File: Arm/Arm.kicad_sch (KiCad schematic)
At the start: 55 parts, among them J10 SparkMAX XT60 F, J11 CAN OUT, J12 SparkMAX XT60 F, J13 SparkMAX XT60 F, J14 Encoder 0, J2 Encoder Bundle, J3 CAN IN, J4 5V Swtich Power, J5 Power IN XT60 M, J6 SparkMAX XT60 F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

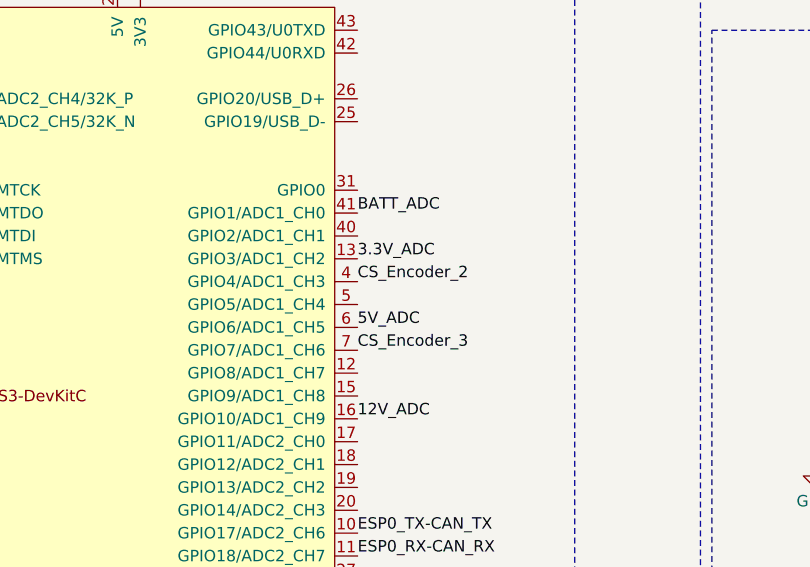
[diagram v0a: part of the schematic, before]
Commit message: Optimizations
Some Labesl

Mounting Holes

Changed some pins around for short traces
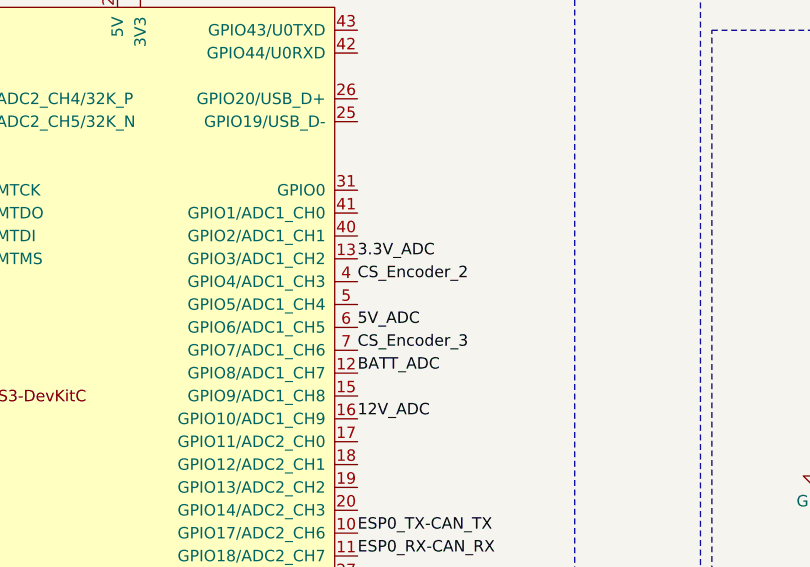
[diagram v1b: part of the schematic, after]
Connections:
- net BATT_ADC: now also U5.12 (GPIO8/ADC1_CH7); no longer U5.41 (GPIO1/ADC1_CH0)
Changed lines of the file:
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@@
+		)
+	)
+	(label "BATT_ADC"
+		(at 73.66 60.96 0)
+		(effects
+			(font
+				(size 1.27 1.27)
+			)
+			(justify left bottom)
 		)
 	)
@@
 		(effects
 			(font
-				(size 1.27 1.27)
-			)
-			(justify left bottom)
-		)
-	)
-	(label "BATT_ADC"
-		(at 73.66 43.18 0)
-		(effects
-			(font

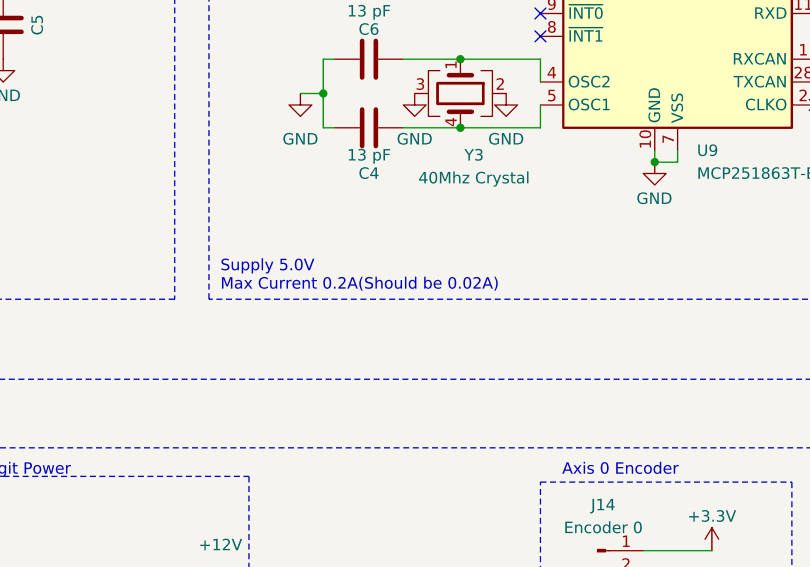
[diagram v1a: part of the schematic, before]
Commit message: Need to swtich to windows
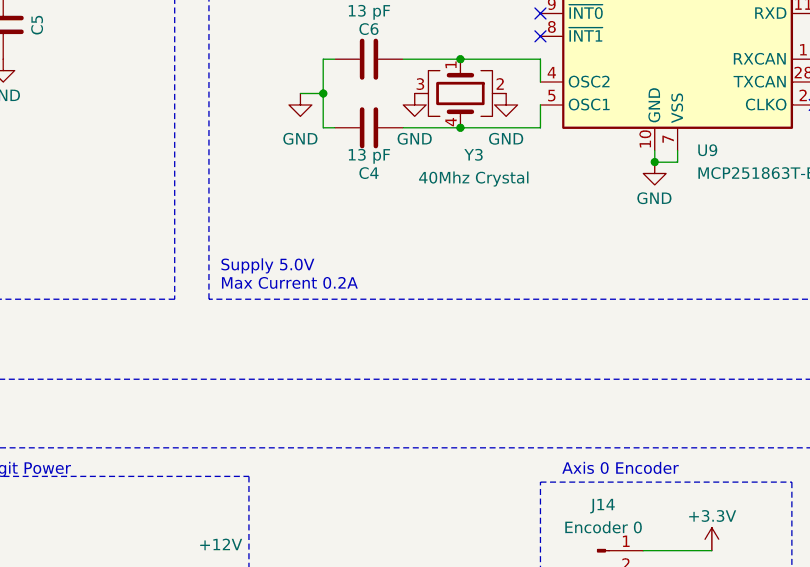
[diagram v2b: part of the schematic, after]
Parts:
- J10: footprint Connector_AMASS:AMASS_XT60-M_1x02_P7.20mm_Vertical -> Connector_AMASS:AMASS_XT60PW-F_1x02_P7.20mm_Horizontal
- J13: footprint Connector_AMASS:AMASS_XT60-F_1x02_P7.20mm_Vertical -> Connector_AMASS:AMASS_XT60PW-F_1x02_P7.20mm_Horizontal
- J5: footprint Connector_AMASS:AMASS_XT60PW-M_1x02_P7.20mm_Horizontal -> Connector_AMASS:AMASS_XT60-M_1x02_P7.20mm_Vertical
- J7: footprint Connector_AMASS:AMASS_XT60PW-F_1x02_P7.20mm_Horizontal -> Connector_AMASS:AMASS_XT60-F_1x02_P7.20mm_Vertical
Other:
- note added: "Supply 5.0V Max Current 0.2A"
- note removed: "Supply 5.0V Max Current 0.2A(Should be 0.02A)"

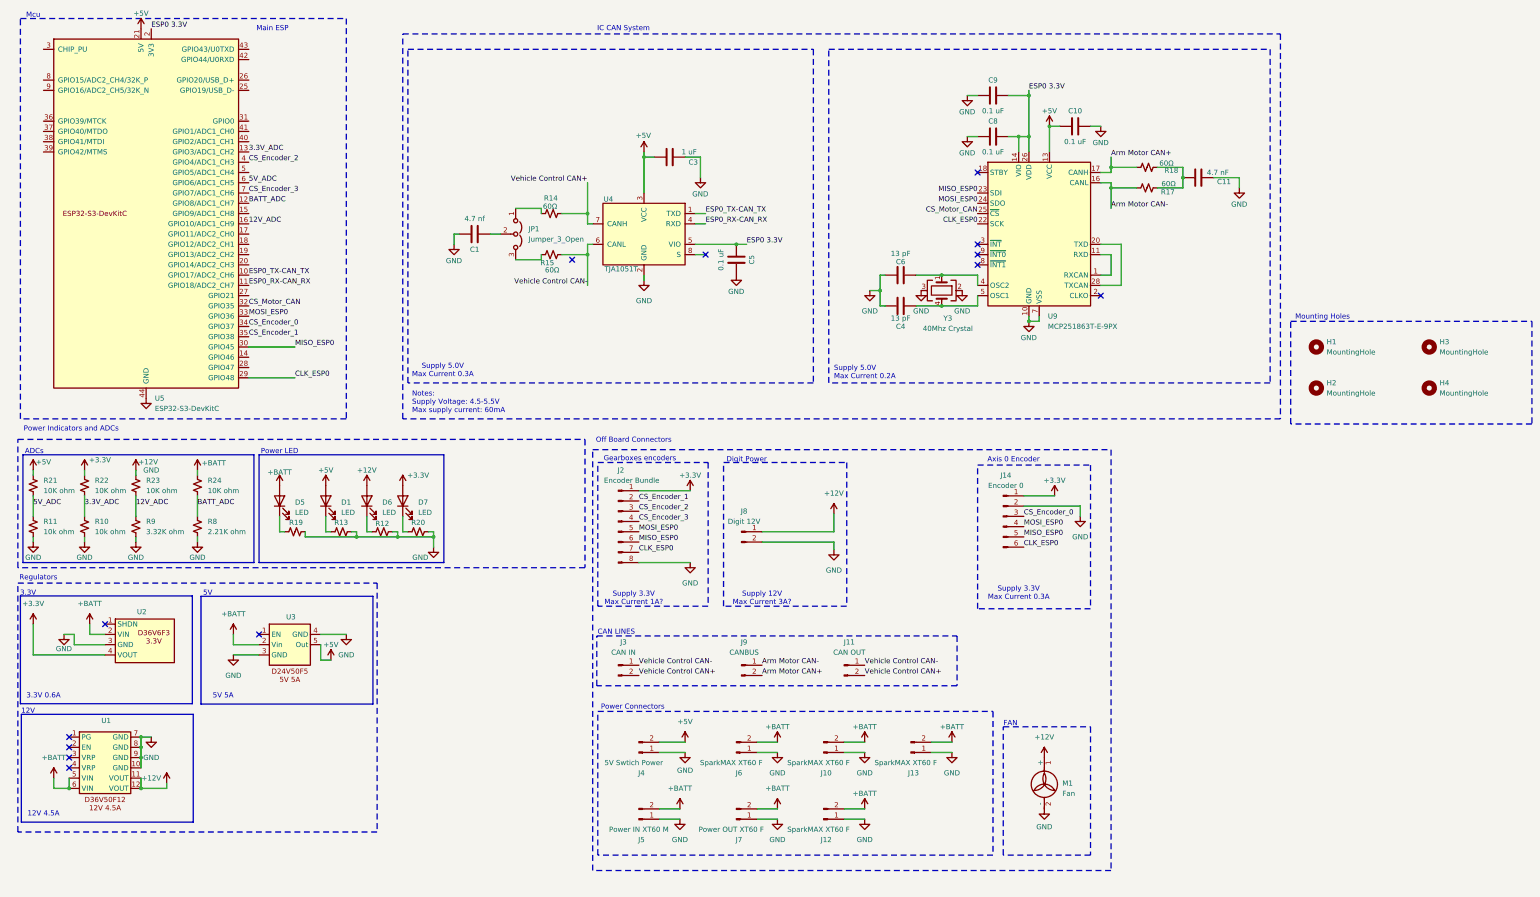
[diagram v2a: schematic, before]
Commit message: Moving Connectors and small layout changes
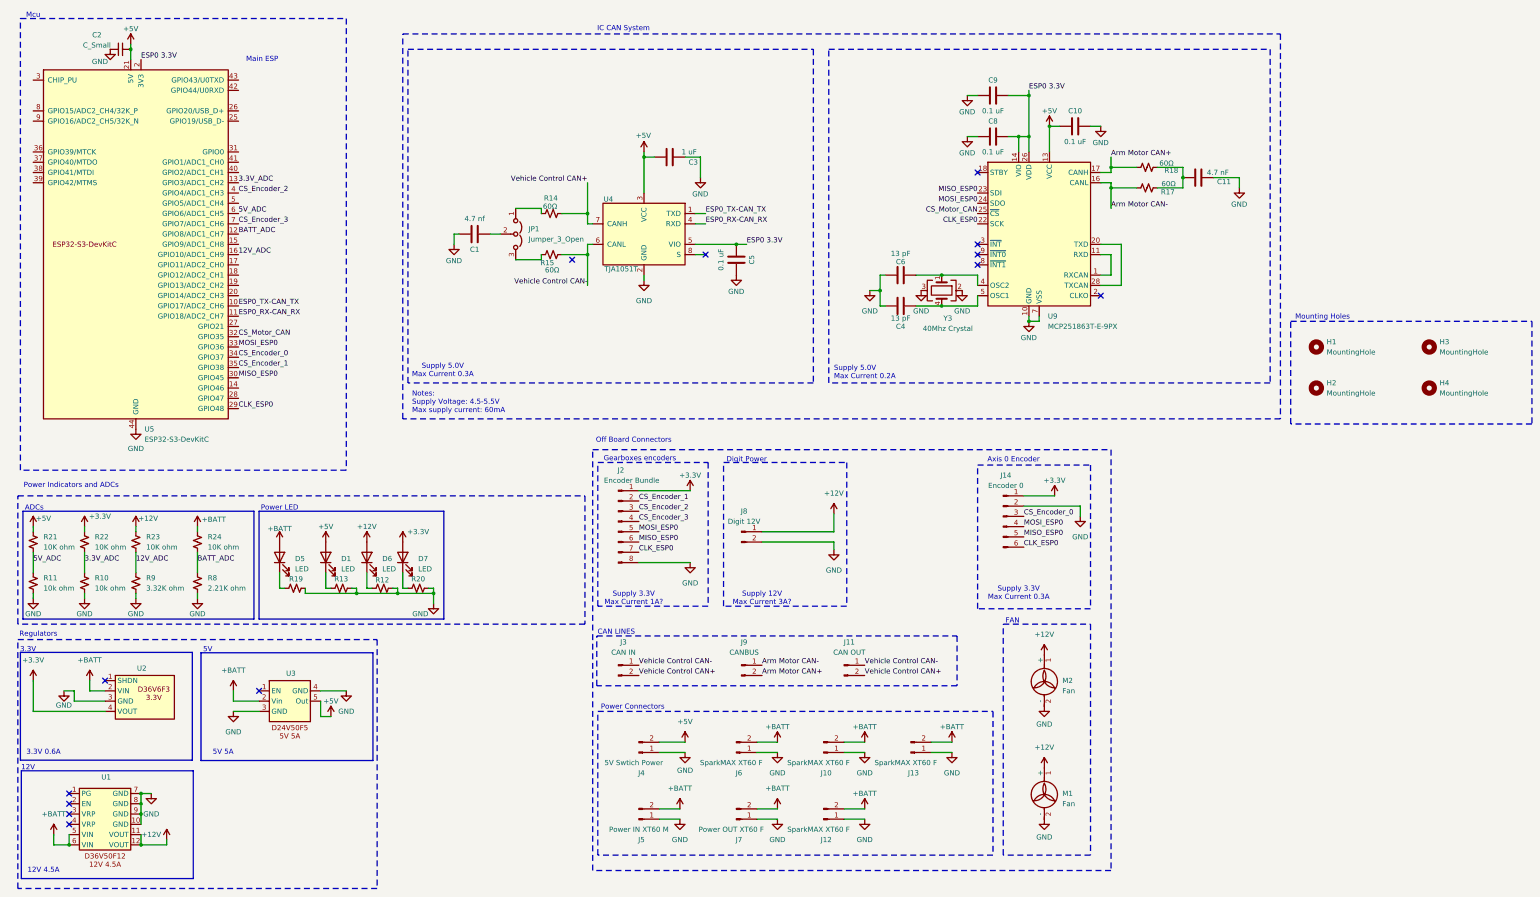
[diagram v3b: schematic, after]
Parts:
- added C2: C_Small, Capacitor_SMD:C_0603_1608Metric_Pad1.08x0.95mm_HandSolder, symbol Device:C_Small
- added M2: Fan, Connector_Molex:Molex_Mini-Fit_Jr_5566-02A_2x01_P4.20mm_Vertical, symbol Motor:Fan
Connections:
- net +12V: now also M2.1 (+)
- net +5V: now also C2.2
- net GND: now also C2.1, M2.2 (-)
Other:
- moved on the sheet: D1, D5, D6, D7, M1, R10, R11, R12, R13, R19, R20, R21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

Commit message: 1/3 Final Changes
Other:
- note added: "Bulk Caps"
- moved on the sheet: C10, C11, C4, C6, C8, C9, R17, R18, U9, Y3

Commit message: 2/3 Final Changes
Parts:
- added C12, C13, C14, C7: C_Small, Capacitor_SMD:C_Elec_4x5.8, symbol Device:C_Small
- J10, J13: footprint Connector_AMASS:AMASS_XT60PW-F_1x02_P7.20mm_Horizontal -> Connector_AMASS:AMASS_XT60-F_1x02_P7.20mm_Vertical
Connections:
- net +BATT: now also C12.1, C13.1, C14.1, C7.1
- net GND: now also C12.2, C13.2, C14.2, C7.2
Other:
- moved on the sheet: J14

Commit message: Final Part 3
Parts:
- removed C12, C13, C14, C7: C_Small, Capacitor_SMD:C_Elec_4x5.8, symbol Device:C_Small
- added C12, C13, C14, C7: 63uF, Capacitor_SMD:CP_Elec_6.3x7.7, symbol Device:C_Polarized_Small
- J12, J6: footprint Connector_AMASS:AMASS_XT60PW-F_1x02_P7.20mm_Horizontal -> Connector_AMASS:AMASS_XT60-F_1x02_P7.20mm_Vertical
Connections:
- net +BATT: now also C12.1, C13.1, C14.1, C7.1
- net GND: now also C12.2, C13.2, C14.2, C7.2

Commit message: Review Changes
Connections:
- net CLK_ESP0: no longer U5.29 (GPIO48)
- net MISO_ESP0: no longer U5.30 (GPIO45)
- net MOSI_ESP0: no longer U5.33 (GPIO36), U9.24 (SDO)
- new net SPI_CLK: U5.29 (GPIO48)
- new net SPI_MISO: U5.30 (GPIO45)
- new net SPI_MOSI: U5.33 (GPIO36)
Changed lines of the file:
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@@
 			"AAAAAAAAAAAAAAAAAAAAAAAAAAAAAAAAAAAAAAAAAAAAAAAAAAAAAAAAAAAAAAAAAAAAAAAAAAAA"
 			"AAAAAAAAAAAAAAAAAAAAAAAAAAAAAAAAAAAAAAAAAAAAAAAAAAAAAAAAAAAAAAAAAAAAAAAAAAAA"
+			"AAAAAAAAAAAAAAAAAAAAAAAAAAAAAAAAAAAAAAAAAAAAAAAAAAAAAAAAAAAAAAAAAAAAAAAAAAAA"
+			"AAAAAAAAAAAAAAAAAAAAAAAAAAAAAAAAAAAAAAAAAAAAAAAAAAAAAAAAAAAAAAAAAAAAAAAAAAAA"
+			"AAAAAAAAAAAAAAAAAAAAAAAAAAAAAAAAAAAAAAAAAAAAAAAAAAAAAAAAAAAAAAAAAAAAAAAAAAAA"
+			"AAAAAAAAAAAAAAAAAAAAAAAAAAAAAAAAAAAAAAAAAAAAAAAAAAAAAAAAAAAAAAAAAAAAAAAAAAAA"
+			"AAAAAAAAAAAAAAAAAAAAAAAAAAAAAAAAAAAAAAAAAAAAAAAAAAAAAAAAAAAAAAAAAAAAAAAAAAAA"
+			"AAAAAAAAAAAAAAAAAAAAAAAAAAAAAAAAAAAAAAAAAAAAAAAAAAAAAAAAAAAAAAAAAAAAAAAAAAAA"
+			"AAAAAAAAAAAAAAAAAAAAAAAAAAAAAAAAAAAAAAAAAAAAAAAAAAAAAAAAAAAAAAAAAAAAAAAAAAAA"
+			"AAAAAAAAAAAAAAAAAAAAAAAAAAAAAAAAAAAAAAAAAAAAAAAAAAAAAAAAAAAAAAAAAAAAAAAAAAAA"
+			"AAAAAAAAAAAAAAAAAAAAAAAAAAAAAAAAAAAAAAAAAAAAAAAAAAAAAAAAAAAAAAAAAAAAAAAAAAAA"
+			"AAAAAAAAAAAAAAAAAAAAAAAAAAAAAAAAAAAAAAAAAAAAAAAAAAAAAAAAAAAAAAAAAAAAAAAAAAAA"
+			"AAAAAAAAAAAAAAAAAAAAAAAAAAAAAAAAAAAAAAAAAAAAAAAAAAAAAAAAAAAAAAAAAAAAAAAAAAAA"
+			"AAAAAAAAAAAAAAAAAAAAAAAAAAAAAAAAAAAAAAAAAAAAAAAAAAAAAAAAAAAAAAAAAAAAAAAAAAAA"
+			"AAAAAAAAAAAAAAAAAAAAAAAAAAAAAAAAAAAAAAAAAAAAAAAAAAAAAAAAAAAAAAAAAAAAAAAAAAAA"
+			"AAAAAAAAAAAAAAAAAAAAAAAAAAAAAAAAAAAAAAAAAAAAAAAAAAAAAAAAAAAAAAAAAAAAAAAAAAAA"
+			"AAAAAAAAAAAAAAAAAAAAAAAAAAAAAAAAAAAAAAAAAAAAAAAAAAAAAAAAAAAAAAAAAAAAAAAAAAAA"
+			"AAAAAAAAAAAAAAAAAAAAAAAAAAAAAAAAAAAAAAAAAAAAAAAAAAAAAAAAAAAAAAAAAAAAAAAAAAAA"
+			"AAAAAAAAAAAAAAAAAAAAAAAAAAAAAAAAAAAAAAAAAAAAAAAAAAAAAAAAAAAAAAAAAAAAAAAAAAAA"
+			"AAAAAAAAAAAAAAAAAAAAAAAAAAAAAAAAAAAAAAAAAAAAAAAAAAAAAAAAAAAAAAAAAAAAAAAAAAAA"
 			"AAAAAAAAAAAAAAAAAAAAAAAAAAAAAAAAAAAAAAAAAAAAAAAAAAAAAAAAAA=="
 		)
@@
 			"AAAAZAAAAGUAAABOAAAAdAAAAFMAAAA4AAAAYgAAAGEAAAAxAAAANAAAADQAAABzAAAAZAAAAEkA"
 			"AABuAAAAbQAAADAAAABJAAAAKwAAAEgAAAA5AAAAWgAAADAAAABrAAAAWAAAAHkAAAA3AAAAZgAA"
-			"AEsAAAArAAAAMwAAAFMAAAB3AAAAbwAAAFUAAABoAAAANQAAAE8AAABkAAAAegAAAA=="
+			"AEsAAAArAAAAMwAAAFMAAAB3AAAAbwAAAFUAAABoAAAANQAAAE8AAABkAAAAegAAAFoAAABHAAAA"
+			"TwAAAE0AAABjAAAAOQAAAGEAAAArAAAARgAAAGYAAABGAAAAUAAAAGgAAABYAAAAeAAAAEQAAAA0"
+			"AAAASQAAADEAAAArAAAAOAAAADgAAABLAAAAKwAAAEsAAAA3AAAARwAAAFQAAABUAAAAZAAAAFcA"
+			"AAAwAAAAOQAAAHgAAABIAAAAYwAAADIAAABzAAAAMgAAAE4AAAA4AAAAVAAAAEYAAABRAAAAdwAA"
+			"AEIAAAAyAAAAawAAAGoAAAA3AAAAcAAAAEIAAAA2AAAAMQAAAEcAAABFAAAANAAAAFMAAAA0AAAA"
+			"ZgAAAHgAAABPAAAAWQAAADQAAAByAAAATAAAADUAAABVAAAAYQAAAGIAAABVAAAAVgAAAEYAAABw"
+			"AAAAUgAAAHUAAABwAAAASwAAAC8AAABOAAAAegAAAFgAAAA5AAAANQAAAHUAAAA2AAAAYQAAAFgA"
+			"AABhAAAAMQAAADEAAABvAAAAUgAAAGgAAABlAAAARwAAAE0AAABqAAAAeAAAAEcAAABQAAAAeAAA"
+			"AE8AAABCAAAAbAAAAFMAAABnAAAAMQAAAEYAAABSAAAAYQAAAHQAAABkAAAAUwAAAFYAAAA3AAAA"
+			"MwAAAHYAAAA3AAAAMgAAADYAAABzAAAAdQAAADEAAAByAAAAcgAAAFEAAAAvAAAAcgAAAEkAAAA4"
+			"AAAASgAAACsAAABLAAAATgAAAEUAAAA4AAAAYgAAAGUAAABHAAAAdAAAAE0AAAA4AAAAWAAAAGUA"
+			"AABHAAAANwAAAGcAAABYAAAAZQAAAGwAAAA2AAAAdgAAAGIAAABSAAAAMwAAAGQAAAByAAAATQAA"
+			"AE8AAABOAAAAMAAAAGMAAABvAAAAeQAAAE0AAABqAAAAcwAAAFIAAAAwAAAASQAAADcAAABFAAAA"
+			"WQAAAHIAAABvAAAASwAAACsAAABTAAAAUAAAADIAAABGAAAANAAAAHIAAAB5AAAATAAAADkAAABs"
+			"AAAAcgAAAHcAAABRAAAATAAAAHcAAABNAAAAcAAAAGEAAABHAAAANwAAAGEAAABNAAAAUAAAADEA"
+			"AAA4AAAAcAAAAHIAAAB1AAAAWQAAAG8AAABSAAAANwAAAEUAAABkAAAAUAAAAGEAAAB2AAAAcgAA"
+			"AGUAAAB2AAAANQAAAHMAAAB6AAAAagAAAEIAAAB4AAAAdwAAAG0AAABQAAAAcgAAAFkAAABXAAAA"
+			"RAAAAHUAAABvAAAAUwAAAGwAAABGAAAAUAAAAHkAAABUAAAAYQAAAFAAAAA1AAAALwAAAHcAAABB"
+			"AAAAMAAAAHcAAABrAAAAYwAAAEwAAABqAAAAYQAAADIAAABHAAAAZwAAADcAAABxAA=="
 		)
 	)
@@
 		)
 	)
-	(label "MISO_ESP0"
+	(label "SPI_MISO"
 		(at 71.12 104.14 0)
 		(effects
@@
 		)
 	)
-	(label "MOSI_ESP0"
-		(at 255.27 55.88 180)
-		(effects
-			(font
-				(size 1.27 1.27)
-			)
-			(justify right bottom)
-		)
-	)
 	(label "CS_Encoder_0"
 		(at 71.12 99.06 0)
@@
 		)
 	)
-	(label "MOSI_ESP0"
+	(label "SPI_MOSI"
 		(at 71.12 96.52 0)
 		(effects
@@
 		)
 	)
-	(label "CLK_ESP0"
+	(label "SPI_CLK"
 		(at 71.12 111.76 0)
 		(effects
